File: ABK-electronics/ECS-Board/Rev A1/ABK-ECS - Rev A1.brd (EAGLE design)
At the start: 80 x 80 mm, 158 parts, among them J1 1241050-5, J2 USB-B-S-RA, J3 22-27-2061-06, J4 22-05-7068-06, J5 22-05-7028-02, J6 22-05-7028-02, J7 22-05-7068-06, K3 G6K-2G-Y, SW1 B3FS-1015, SW2 B3FS-1015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

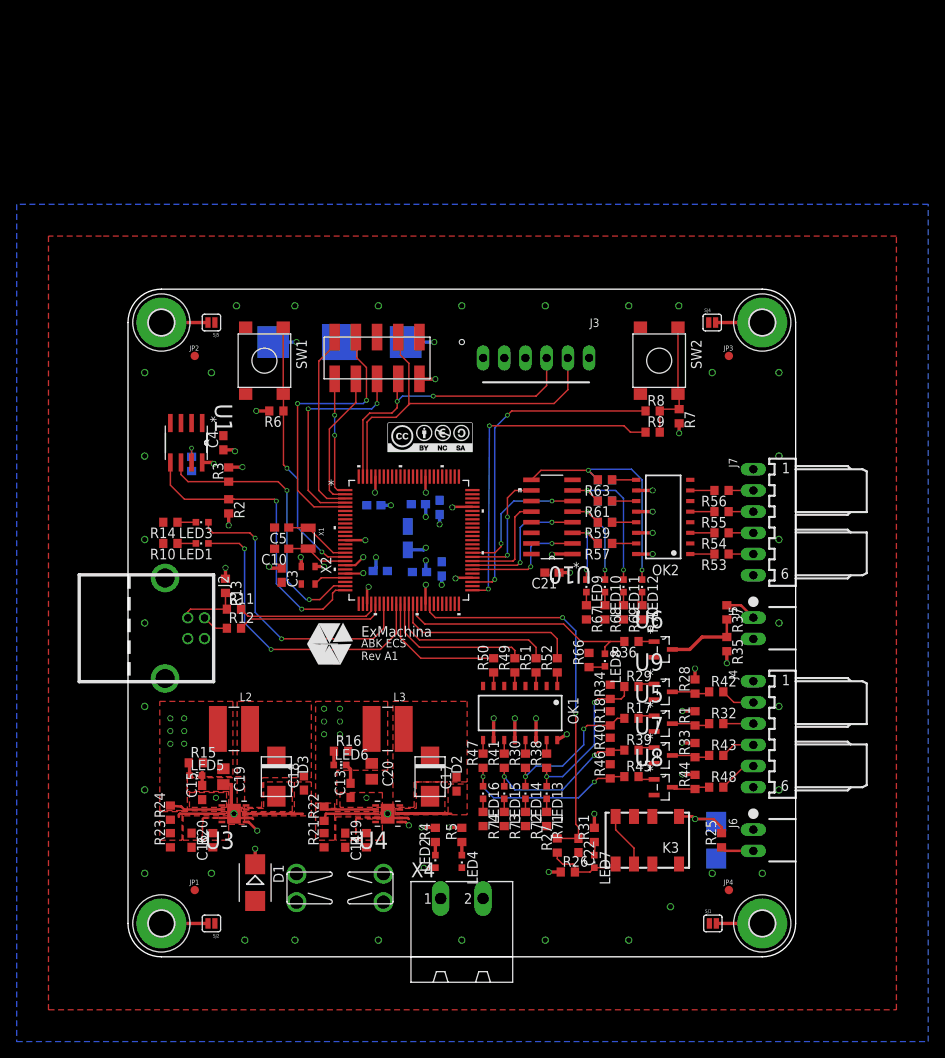
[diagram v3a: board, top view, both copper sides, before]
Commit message: Add Silkscreen
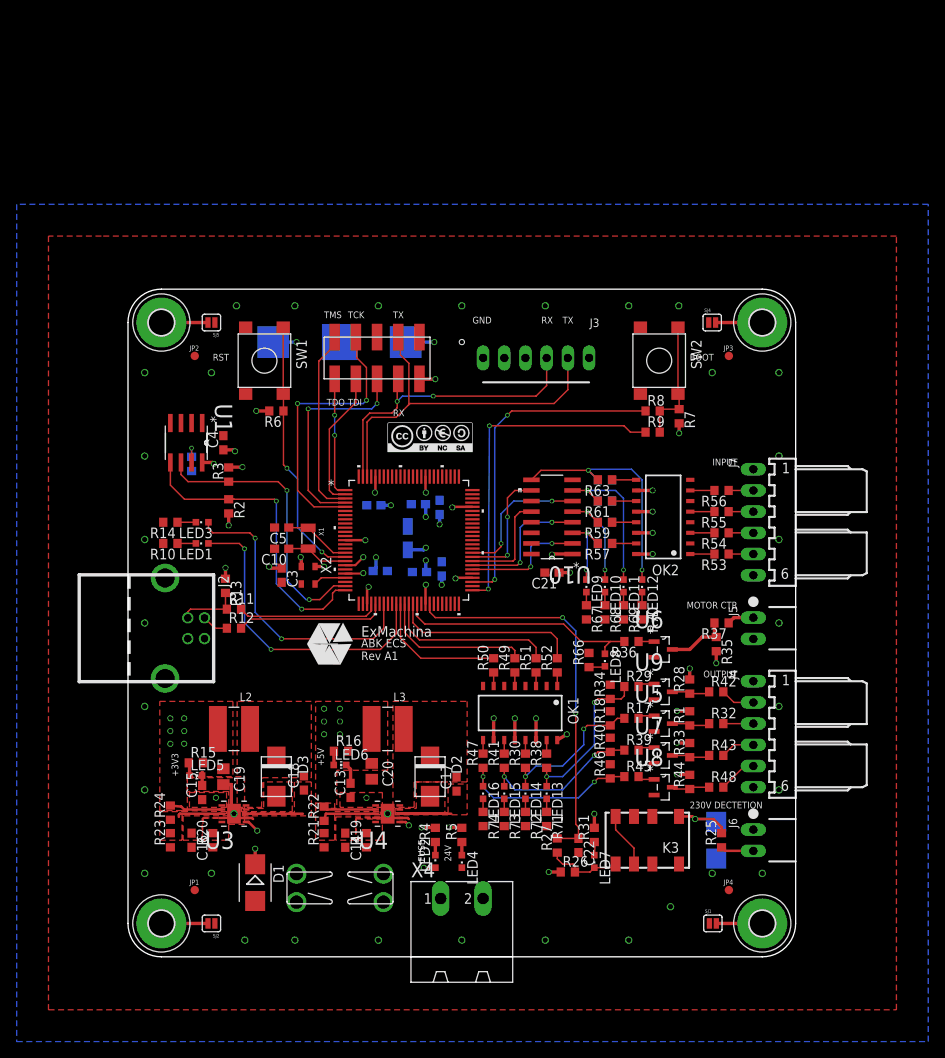
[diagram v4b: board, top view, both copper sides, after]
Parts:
- moved R37 1.42 mm to (71.1, 40.0), turned to 180 degrees
- moved R35 1.27 mm to (70.5, 37.5)
- moved R1 0.63 mm to (67.3, 28.6)
- moved R28 0.63 mm to (67.3, 32.4)
- moved R33 0.63 mm to (67.3, 24.8)
- moved R44 0.63 mm to (67.3, 21.0)
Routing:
- net N$24: track 9.25 -> 7.65 mm
- net N$26: track 3.79 -> 3.22 mm
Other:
- board text added: "+3V3"
- board text added: "+5V"
- board text added: "230V DECTETION"
- board text added: "24V"
- board text added: "BOOT"
- board text added: "FUSE"
- board text added: "GND"
- board text added: "INPUT"
- board text added: "MOTOR CTR"
- board text added: "OUTPUT"
- board text added: "RST"
- board text added: "RX"
- board text added: "TCK"
- board text added: "TDI"
- board text added: "TDO"
- board text added: "TMS"
- board text added: "TX"

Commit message: Add component reference
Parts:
- LED2: value Blue -> Red
- R15, R16: value 1k5 -> 1K5
- R19, R20, R24: value 31k6 -> 31K6
- R21, R23: value 10k -> 10K
- R22: value 52k3 -> 52K3
- R4, R5: value 4k7 -> 4K7

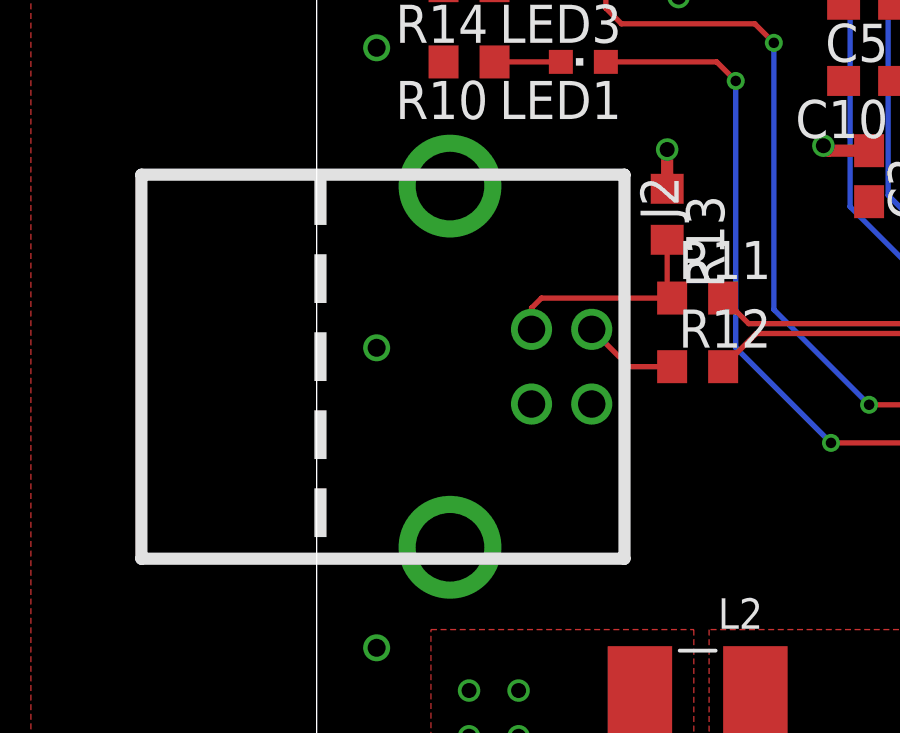
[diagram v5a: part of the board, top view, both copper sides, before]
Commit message: Add solderJump to the usb shield and replace layer 3 into 15
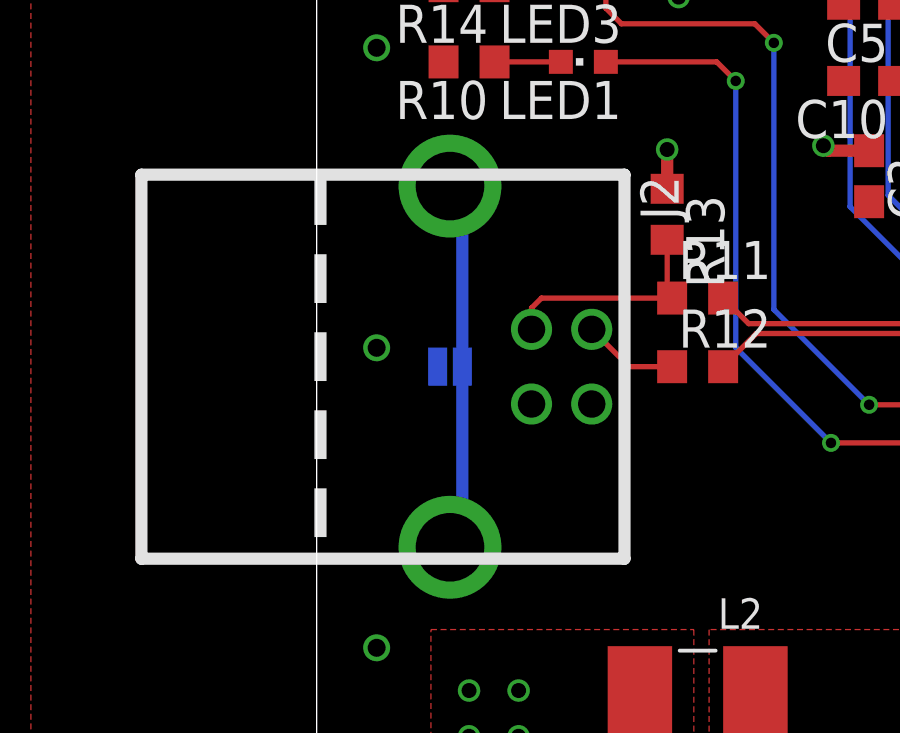
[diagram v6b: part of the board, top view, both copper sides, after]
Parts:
- added SJ3: SOLDERJUMPERNC, SparkFun-Passives:SJ_2S
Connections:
- new net N$70: J2.SHL, J2.SHL1, SJ3.2
- net GND: now also SJ3.1
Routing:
- net N$70: track 0.00 -> 12.4 mm
- added copper zone on layer 15, net +24V
- added copper zone on layer 15, net +3V3
- added copper zone on layer 15, net +5V
- added copper zone on layer 15, net VIN
- removed copper zone on layer 3, net +24V
- removed copper zone on layer 3, net +3V3
- removed copper zone on layer 3, net +5V
- removed copper zone on layer 3, net VIN
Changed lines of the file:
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@@
 <layer number="1" name="Top" color="16" fill="1" visible="yes" active="yes"/>
 <layer number="2" name="Route2" color="17" fill="1" visible="yes" active="yes"/>
-<layer number="3" name="Route3" color="39" fill="1" visible="yes" active="yes"/>
 <layer number="14" name="Route14" color="1" fill="6" visible="no" active="no"/>
-<layer number="15" name="Route15" color="19" fill="6" visible="no" active="no"/>
-<layer number="16" name="Bottom" color="21" fill="1" visible="no" active="yes"/>
+<layer number="15" name="Route15" color="19" fill="1" visible="yes" active="yes"/>
+<layer number="16" name="Bottom" color="21" fill="1" visible="yes" active="yes"/>
 <layer number="17" name="Pads" color="18" fill="1" visible="yes" active="yes"/>
 <layer number="18" name="Vias" color="38" fill="1" visible="yes" active="yes"/>
@@
 <layer number="20" name="Dimension" color="7" fill="1" visible="yes" active="yes"/>
 <layer number="21" name="tPlace" color="55" fill="1" visible="yes" active="yes"/>
-<layer number="22" name="bPlace" color="54" fill="1" visible="no" active="yes"/>
+<layer number="22" name="bPlace" color="54" fill="1" visible="yes" active="yes"/>
 <layer number="23" name="tOrigins" color="15" fill="1" visible="yes" active="yes"/>
-<layer number="24" name="bOrigins" color="15" fill="1" visible="no" active="yes"/>
+<layer number="24" name="bOrigins" color="15" fill="1" visible="yes" active="yes"/>
 <layer number="25" name="tNames" color="55" fill="1" visible="no" active="yes"/>
 <layer number="26" name="bNames" color="54" fill="1" visible="no" active="yes"/>
@@
 <layer number="37" name="tTest" color="7" fill="1" visible="no" active="yes"/>
 <layer number="38" name="bTest" color="7" fill="1" visible="no" active="yes"/>
-<layer number="39" name="tKeepout" color="4" fill="11" visible="yes" active="yes"/>
-<layer number="40" name="bKeepout" color="3" fill="11" visible="yes" active="yes"/>
-<layer number="41" name="tRestrict" color="4" fill="10" visible="yes" active="yes"/>
-<layer number="42" name="bRestrict" color="3" fill="10" visible="yes" active="yes"/>
-<layer number="43" name="vRestrict" color="2" fill="10" visible="yes" active="yes"/>
+<layer number="39" name="tKeepout" color="4" fill="11" visible="no" active="yes"/>
+<layer number="40" name="bKeepout" color="3" fill="11" visible="no" active="yes"/>
+<layer number="41" name="tRestrict" color="4" fill="10" visible="no" active="yes"/>
+<layer number="42" name="bRestrict" color="3" fill="10" visible="no" active="yes"/>
+<layer number="43" name="vRestrict" color="2" fill="10" visible="no" active="yes"/>
 <layer number="44" name="Drills" color="16" fill="1" visible="no" active="yes"/>
 <layer number="45" name="Holes" color="35" fill="1" visible="no" active="yes"/>
@@
 <layer number="49" name="Reference" color="48" fill="1" visible="yes" active="yes"/>
 <layer number="50" name="dxf" color="7" fill="1" visible="yes" active="yes"/>
-<layer number="51" name="tDocu" color="55" fill="1" visible="yes" active="yes"/>
-<layer number="52" name="bDocu" color="54" fill="1" visible="no" active="yes"/>
+<layer number="51" name="tDocu" color="55" fill="1" visible="no" active="yes"/>
+<layer number="52" name="bDocu" color="54" fill="1" visible="yes" active="yes"/>
 <layer number="53" name="tGND_GNDA" color="7" fill="1" visible="yes" active="yes"/>
 <layer number="54" name="bGND_GNDA" color="7" fill="1" visible="yes" active="yes"/>
@@
 </class>
 </classes>
-<designrules name="eC_4Layer_PClass6_BaseCopperO18-I35_eCDefault">
+<designrules name="eC_4Layer_PClass6_BaseCopperO18-I35_eCDefault *">
 <description language="de">
 &lt;p&gt;
@@
 Your Eurocircuits Team
 </description>
-<param name="layerSetup" value="(1+2*3+16)"/>
+<param name="layerSetup" value="(1+2*15+16)"/>
 <param name="mtCopper" value="0.018mm 0.035mm 0.035mm 0.035mm 0.035mm 0.035mm 0.035mm 0.035mm 0.035mm 0.035mm 0.035mm 0.035mm 0.035mm 0.035mm 0.035mm 0.018mm"/>
 <param name="mtIsolate" value="0.36mm 0.71mm 0.36mm 0.2mm 0.2mm 0.2mm 0.2mm 0.15mm 0.2mm 0.15mm 0.2mm 0.15mm 0.2mm 0.15mm 0.2mm"/>
@@
 <attribute name="OC_NEWARK" value="86T3542" x="49.53" y="30.48" size="1.778" layer="27" rot="R90" display="off"/>
 </element>
+<element name="SJ3" library="SparkFun-Passives" package="SJ_2S" value="SOLDERJUMPERNC" x="4.445" y="39.37" rot="MR180"/>
 </elements>
 <signals>
@@
 <contactref element="R74" pad="2"/>
 <contactref element="R66" pad="2"/>
+<contactref element="SJ3" pad="1"/>
 </signal>
 <signal name="+3V3" class="2">
@@
 <contactref element="U10" pad="1"/>
 <contactref element="C21" pad="1"/>
-<polygon width="0.4064" layer="3" isolate="0.1778" rank="6">
+<polygon width="0.4064" layer="15" isolate="0.1778" rank="6">
 <vertex x="-12.065" y="-8.89"/>
 <vertex x="94.615" y="-8.89"/>
@@
 <wire x1="26.03" y1="45.92" x2="28.14" y2="45.92" width="0.254" layer="1"/>
 <wire x1="28.14" y1="45.92" x2="28.194" y2="45.974" width="0.254" layer="1"/>
-<wire x1="9.1694" y1="38.1254" x2="13.9954" y2="38.1254" width="0.254" layer="3"/>
-<wire x1="13.9954" y1="38.1254" x2="21.844" y2="45.974" width="0.254" layer="3"/>
-<wire x1="21.844" y1="45.974" x2="28.194" y2="45.974" width="0.254" layer="3"/>
+<wire x1="9.1694" y1="38.1254" x2="13.9954" y2="38.1254" width="0.254" layer="15"/>
+<wire x1="13.9954" y1="38.1254" x2="21.844" y2="45.974" width="0.254" layer="15"/>
+<wire x1="21.844" y1="45.974" x2="28.194" y2="45.974" width="0.254" layer="15"/>
 </signal>
 <signal name="USB_UP_LED" class="1">
@@
 <wire x1="36.703" y1="73.66" x2="33.274" y2="73.66" width="0.4064" layer="16"/>
 <wire x1="20.193" y1="73.66" x2="17.399" y2="73.66" width="0.4064" layer="16"/>
-<wire x1="20.193" y1="73.66" x2="22.86" y2="70.993" width="0.4064" layer="3"/>
-<wire x1="22.86" y1="70.993" x2="22.86" y2="53.213" width="0.4064" layer="3"/>
-<wire x1="22.86" y1="53.213" x2="28.194" y2="47.879" width="0.4064" layer="3"/>
+<wire x1="20.193" y1="73.66" x2="22.86" y2="70.993" width="0.4064" layer="15"/>
+<wire x1="22.86" y1="70.993" x2="22.86" y2="53.213" width="0.4064" layer="15"/>
+<wire x1="22.86" y1="53.213" x2="28.194" y2="47.879" width="0.4064" layer="15"/>
 <via x="28.194" y="47.879" extent="1-16" drill="0.5"/>
 <wire x1="28.194" y1="47.879" x2="27.235" y2="46.92" width="0.254" layer="1"/>
 <wire x1="27.235" y1="46.92" x2="26.03" y2="46.92" width="0.254" layer="1"/>
-<wire x1="22.86" y1="70.993" x2="25.527" y2="73.66" width="0.4064" layer="3"/>
-<wire x1="25.527" y1="73.66" x2="36.703" y2="73.66" width="0.4064" layer="3"/>
+<wire x1="22.86" y1="70.993" x2="25.527" y2="73.66" width="0.4064" layer="15"/>
+<wire x1="25.527" y1="73.66" x2="36.703" y2="73.66" width="0.4064" layer="15"/>
 </signal>
 <signal name="N$5" class="1">
@@
 <contactref element="F1" pad="1"/>
 <contactref element="LED2" pad="A"/>
-<polygon width="0.4064" layer="3">
+<polygon width="0.4064" layer="15">
 <vertex x="24.765" y="11.938"/>
 <vertex x="24.892" y="4.445"/>
@@
 <contactref element="R44" pad="2"/>
 <contactref element="J7" pad="1"/>
-<polygon width="0.4064" layer="3">
+<polygon width="0.4064" layer="15">
 <vertex x="82.55" y="8.89"/>
 <vertex x="64.77" y="8.89"/>
@@
 <vertex x="7.366" y="17.907"/>
 </polygon>
-<polygon width="0.4064" layer="3" rank="3">
+<polygon width="0.4064" layer="15" rank="3">
 <vertex x="67.945" y="3.175"/>
 <vertex x="9.398" y="3.175"/>
@@
 <via x="50.419" y="10.16" extent="1-16" drill="0.5"/>
 <wire x1="51.855" y1="10.16" x2="50.419" y2="10.16" width="0.4064" layer="1"/>
-<polygon width="0.4064" layer="3" rank="2">
+<polygon width="0.4064" layer="15" rank="2">
 <vertex x="22.225" y="31.115"/>
 <vertex x="59.69" y="31.115"/>
@@
 <wire x1="57.05" y1="34.71" x2="57.15" y2="34.81" width="0.1778" layer="1"/>
 </signal>
+<signal name="N$70">
+<contactref element="SJ3" pad="2"/>
+<contactref element="J2" pad="SHL1"/>
+<contactref element="J2" pad="SHL"/>
+<wire x1="4.445" y1="33.3502" x2="4.8569" y2="33.7621" width="0.4064" layer="16"/>
+<wire x1="4.8569" y1="33.7621" x2="4.8569" y2="39.37" width="0.4064" layer="16"/>
+<wire x1="4.445" y1="45.3898" x2="4.8569" y2="44.9779" width="0.4064" layer="16"/>
+<wire x1="4.8569" y1="44.9779" x2="4.8569" y2="39.37" width="0.4064" layer="16"/>
+</signal>
 </signals>

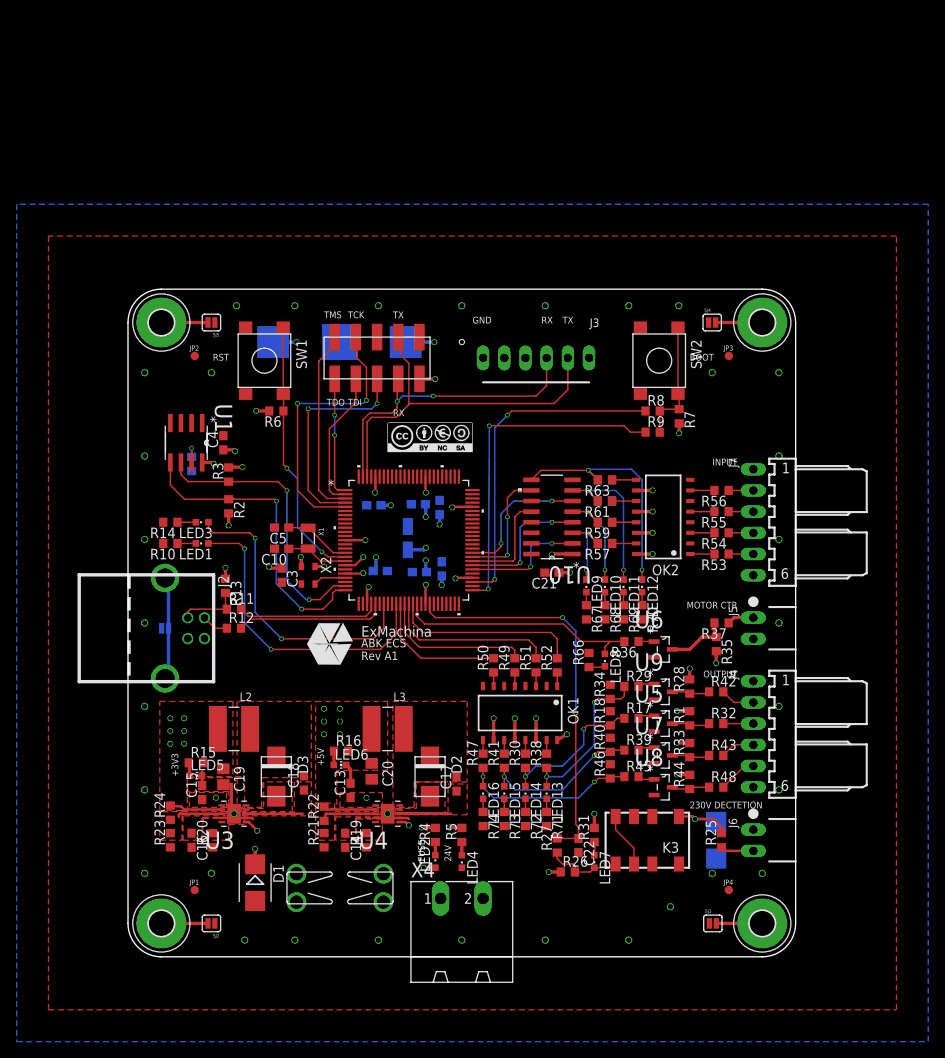
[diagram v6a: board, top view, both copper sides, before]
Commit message: Add MDP files
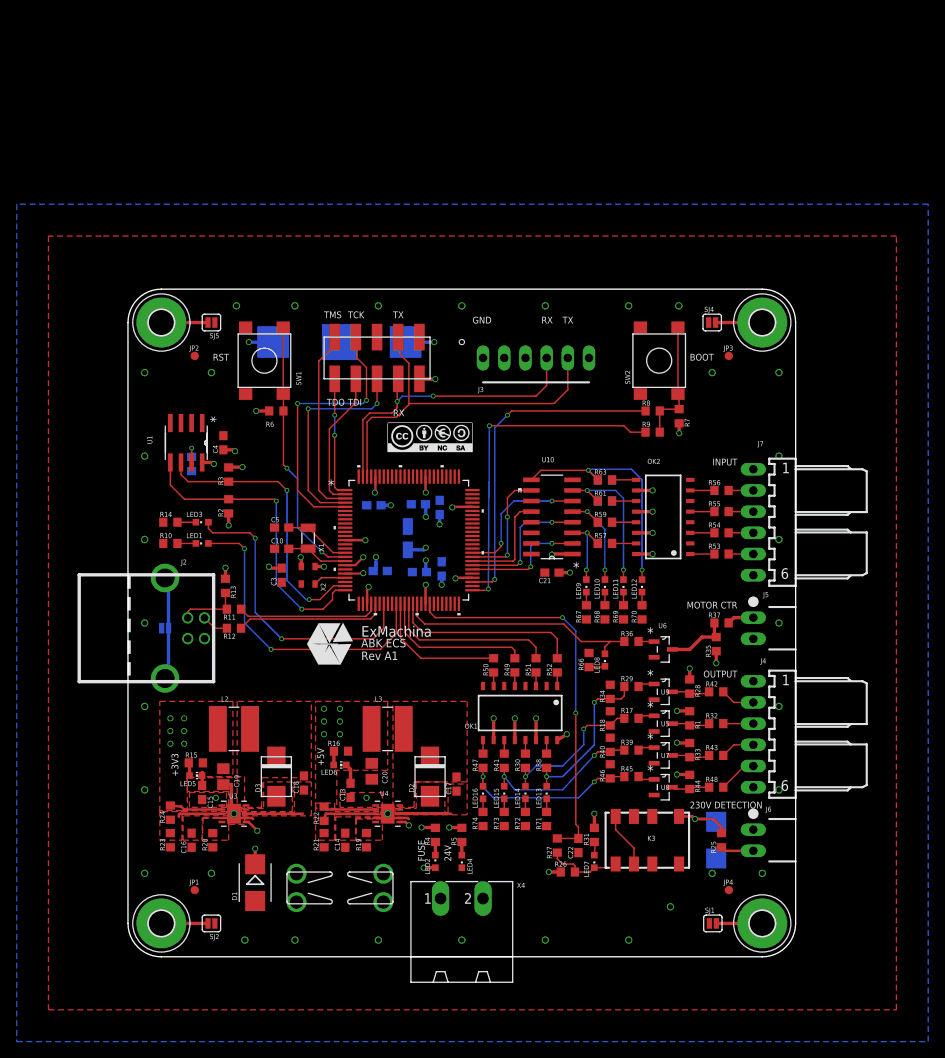
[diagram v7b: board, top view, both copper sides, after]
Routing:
- net VBAT+: track 52.8 -> 58.7 mm
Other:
- board text added: "230V DETECTION"
- board text removed: "230V DECTETION"
